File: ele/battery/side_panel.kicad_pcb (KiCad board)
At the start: 2 copper layers, 46.8 x 87.2 mm, 36 parts, among them J1 banana, J10 B1_trans, J11 B2_trans, J2 banana, J3 banana, J4 banana, J5 B1_sping, J6 B2_sping, J9 mech

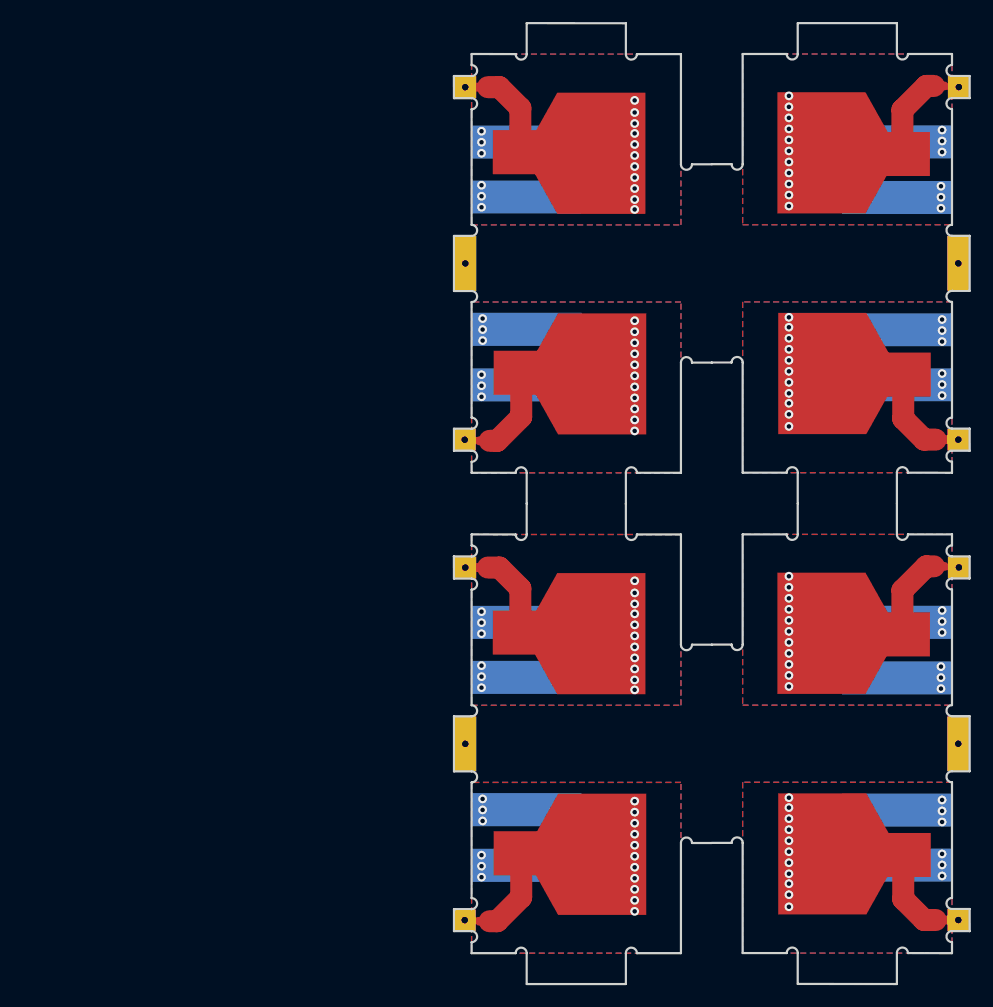
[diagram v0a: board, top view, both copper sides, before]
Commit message: ele: Update battery panels
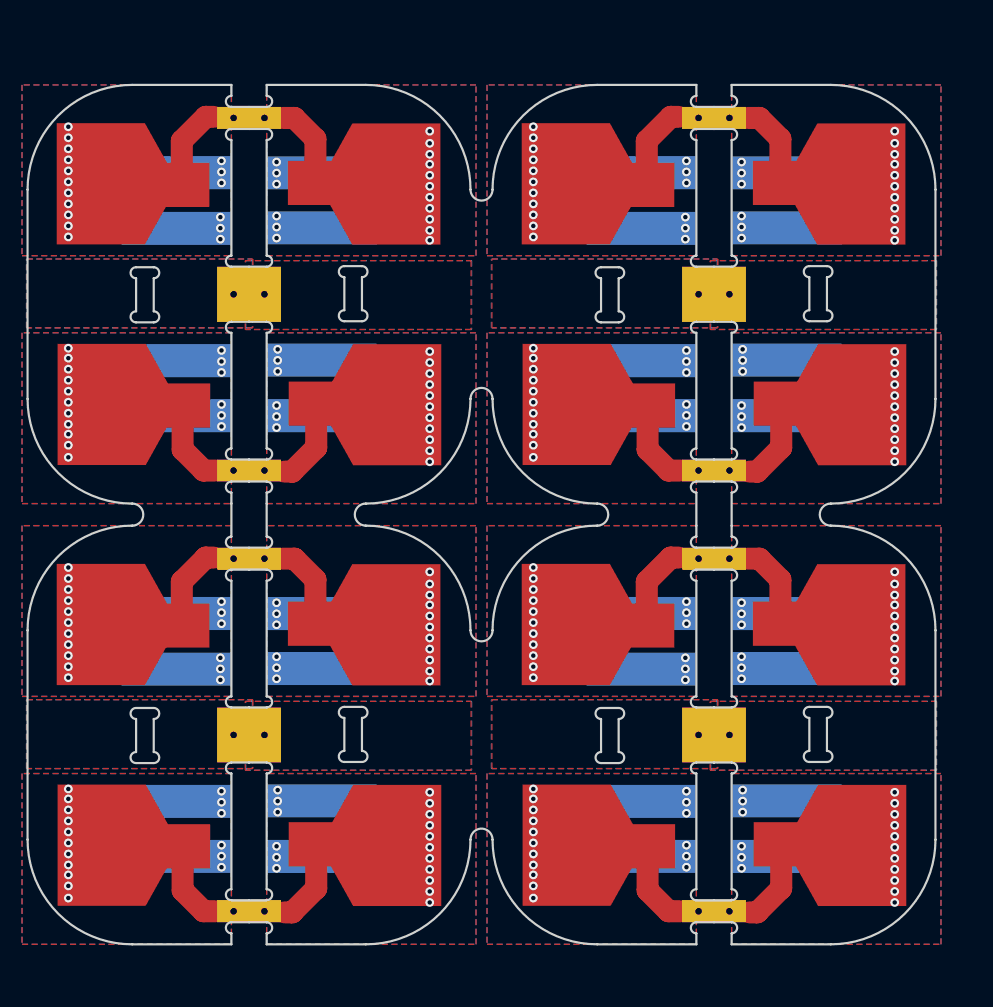
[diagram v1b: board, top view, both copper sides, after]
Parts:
- removed the J1 at (145.8, 141.2)
- removed the J1 at (112.2, 129.2)
- removed the J1 at (145.8, 97.6)
- removed the J1 at (112.2, 85.6)
- removed the J10 at (106.6, 119.2)
- removed the J10 at (151.4, 151.2)
- removed the J10 at (151.4, 107.6)
- removed the J10 at (106.6, 75.6)
- removed the J11 at (106.6, 151.2)
- removed the J11 at (151.4, 119.2)
- removed the J11 at (151.4, 75.6)
- removed the J11 at (106.6, 107.6)
- removed the J2 at (145.8, 146.2)
- removed the J2 at (112.2, 124.2)
- removed the J2 at (145.8, 102.6)
- removed the J2 at (112.2, 80.6)
- removed the J3 at (112.2, 146.2)
- removed the J3 at (145.8, 124.2)
- removed the J3 at (145.8, 80.6)
- removed the J3 at (112.2, 102.6)
- removed the J4 at (145.8, 129.2)
- removed the J4 at (112.2, 141.2)
- removed the J4 at (145.8, 85.6)
- removed the J4 at (112.2, 97.6)
- removed the J5 at (140.6, 145.3)
- removed the J5 at (117.4, 125.1)
- removed the J5 at (140.6, 101.7)
- removed the J5 at (117.4, 81.5)
- removed the J6 at (117.5, 145.1)
- removed the J6 at (140.5, 125.3)
- removed the J6 at (140.5, 81.7)
- removed the J6 at (117.5, 101.5)
- removed the J9 at (106.6, 135.2)
- removed the J9 at (151.4, 135.2)
- removed the J9 at (151.4, 91.6)
- removed the J9 at (106.6, 91.6)
- added J1: banana, yaqwsx:banana_2mm_side, B.Cu at (80.4, 100.4)
- added J1: banana, yaqwsx:banana_2mm_side, B.Cu at (93.6, 88.4)
- added J1: banana, yaqwsx:banana_2mm_side, B.Cu at (93.6, 128.4)
- added J1: banana, yaqwsx:banana_2mm_side, B.Cu at (80.4, 140.4)
- added J1: banana, yaqwsx:banana_2mm_side, B.Cu at (135.8, 128.4)
- added J1: banana, yaqwsx:banana_2mm_side, B.Cu at (122.6, 140.4)
- added J1: banana, yaqwsx:banana_2mm_side, B.Cu at (122.6, 100.4)
- added J1: banana, yaqwsx:banana_2mm_side, B.Cu at (135.8, 88.4)
- added J10: B1_trans, yaqwsx:pad_2x3, F.Cu at (85.6, 110.4)
- added J10: B1_trans, yaqwsx:pad_2x3, F.Cu at (88.4, 78.4)
- added J10: B1_trans, yaqwsx:pad_2x3, F.Cu at (88.4, 118.4)
- added J10: B1_trans, yaqwsx:pad_2x3, F.Cu at (85.6, 150.4)
- added J10: B1_trans, yaqwsx:pad_2x3, F.Cu at (130.6, 118.4)
- added J10: B1_trans, yaqwsx:pad_2x3, F.Cu at (127.8, 150.4)
- added J10: B1_trans, yaqwsx:pad_2x3, F.Cu at (127.8, 110.4)
- added J10: B1_trans, yaqwsx:pad_2x3, F.Cu at (130.6, 78.4)
- added J11: B2_trans, yaqwsx:pad_2x3, F.Cu at (85.6, 78.4)
- added J11: B2_trans, yaqwsx:pad_2x3, F.Cu at (88.4, 110.4)
- added J11: B2_trans, yaqwsx:pad_2x3, F.Cu at (88.4, 150.4)
- added J11: B2_trans, yaqwsx:pad_2x3, F.Cu at (85.6, 118.4)
- added J11: B2_trans, yaqwsx:pad_2x3, F.Cu at (130.6, 150.4)
- added J11: B2_trans, yaqwsx:pad_2x3, F.Cu at (127.8, 118.4)
- added J11: B2_trans, yaqwsx:pad_2x3, F.Cu at (127.8, 78.4)
- added J11: B2_trans, yaqwsx:pad_2x3, F.Cu at (130.6, 110.4)
- added J2: banana, yaqwsx:banana_2mm_side, B.Cu at (93.6, 83.4)
- added J2: banana, yaqwsx:banana_2mm_side, B.Cu at (80.4, 105.4)
- added J2: banana, yaqwsx:banana_2mm_side, B.Cu at (80.4, 145.4)
- added J2: banana, yaqwsx:banana_2mm_side, B.Cu at (93.6, 123.4)
- added J2: banana, yaqwsx:banana_2mm_side, B.Cu at (122.6, 145.4)
- added J2: banana, yaqwsx:banana_2mm_side, B.Cu at (135.8, 123.4)
- added J2: banana, yaqwsx:banana_2mm_side, B.Cu at (122.6, 105.4)
- added J2: banana, yaqwsx:banana_2mm_side, B.Cu at (135.8, 83.4)
- added J3: banana, yaqwsx:banana_2mm_side, B.Cu at (80.4, 83.4)
- added J3: banana, yaqwsx:banana_2mm_side, B.Cu at (93.6, 145.4)
- added J3: banana, yaqwsx:banana_2mm_side, B.Cu at (93.6, 105.4)
- added J3: banana, yaqwsx:banana_2mm_side, B.Cu at (80.4, 123.4)
- added J3: banana, yaqwsx:banana_2mm_side, B.Cu at (135.8, 145.4)
- added J3: banana, yaqwsx:banana_2mm_side, B.Cu at (122.6, 123.4)
- added J3: banana, yaqwsx:banana_2mm_side, B.Cu at (122.6, 83.4)
- added J3: banana, yaqwsx:banana_2mm_side, B.Cu at (135.8, 105.4)
- added J4: banana, yaqwsx:banana_2mm_side, B.Cu at (80.4, 88.4)
- added J4: banana, yaqwsx:banana_2mm_side, B.Cu at (93.6, 100.4)
- added J4: banana, yaqwsx:banana_2mm_side, B.Cu at (93.6, 140.4)
- added J4: banana, yaqwsx:banana_2mm_side, B.Cu at (80.4, 128.4)
- added J4: banana, yaqwsx:banana_2mm_side, B.Cu at (135.8, 140.4)
- added J4: banana, yaqwsx:banana_2mm_side, B.Cu at (122.6, 128.4)
- added J4: banana, yaqwsx:banana_2mm_side, B.Cu at (122.6, 88.4)
- added J4: banana, yaqwsx:banana_2mm_side, B.Cu at (135.8, 100.4)
- added J5: B1_sping, yaqwsx:battery_spring_contact, F.Cu at (98.8, 84.3)
- added J5: B1_sping, yaqwsx:battery_spring_contact, F.Cu at (75.2, 104.5)
- added J5: B1_sping, yaqwsx:battery_spring_contact, F.Cu at (98.8, 124.3)
- added J5: B1_sping, yaqwsx:battery_spring_contact, F.Cu at (75.2, 144.5)
- added J5: B1_sping, yaqwsx:battery_spring_contact, F.Cu at (141.0, 124.3)
- added J5: B1_sping, yaqwsx:battery_spring_contact, F.Cu at (117.4, 144.5)
- added J5: B1_sping, yaqwsx:battery_spring_contact, F.Cu at (117.4, 104.5)
- added J5: B1_sping, yaqwsx:battery_spring_contact, F.Cu at (141.0, 84.3)
- added J6: B2_sping, yaqwsx:battery_spring_contact, F.Cu at (75.1, 84.5)
- added J6: B2_sping, yaqwsx:battery_spring_contact, F.Cu at (98.9, 104.3)
- added J6: B2_sping, yaqwsx:battery_spring_contact, F.Cu at (98.9, 144.3)
- added J6: B2_sping, yaqwsx:battery_spring_contact, F.Cu at (75.1, 124.5)
- added J6: B2_sping, yaqwsx:battery_spring_contact, F.Cu at (141.1, 144.3)
- added J6: B2_sping, yaqwsx:battery_spring_contact, F.Cu at (117.3, 124.5)
- added J6: B2_sping, yaqwsx:battery_spring_contact, F.Cu at (117.3, 84.5)
- added J6: B2_sping, yaqwsx:battery_spring_contact, F.Cu at (141.1, 104.3)
- added J9: mech, BATTERY:pad_3x5, F.Cu at (88.4, 94.4)
- added J9: mech, BATTERY:pad_3x5, F.Cu at (85.6, 94.4)
- added J9: mech, BATTERY:pad_3x5, F.Cu at (85.6, 134.4)
- added J9: mech, BATTERY:pad_3x5, F.Cu at (88.4, 134.4)
- added J9: mech, BATTERY:pad_3x5, F.Cu at (127.8, 134.4)
- added J9: mech, BATTERY:pad_3x5, F.Cu at (130.6, 134.4)
- added J9: mech, BATTERY:pad_3x5, F.Cu at (127.8, 94.4)
- added J9: mech, BATTERY:pad_3x5, F.Cu at (130.6, 94.4)
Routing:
- net /B1_trans: track 76.7 -> 153.4 mm, vias 44 -> 88
- net /B2_trans: track 49.5 -> 99.0 mm, vias 44 -> 88
- net Net-(J4-Pad1): vias 12 -> 24
- net Net-(J3-Pad1): vias 12 -> 24
- net Net-(J2-Pad1): vias 12 -> 24
- net Net-(J1-Pad1): vias 12 -> 24
- added copper zone on B.Cu, net Net-(J9-Pad1)
- added copper zone on F.Cu, net Net-(J9-Pad1)
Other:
- board size 46.8 x 87.2 mm -> 82.4 x 78 mm

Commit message: ele: Update battery panels
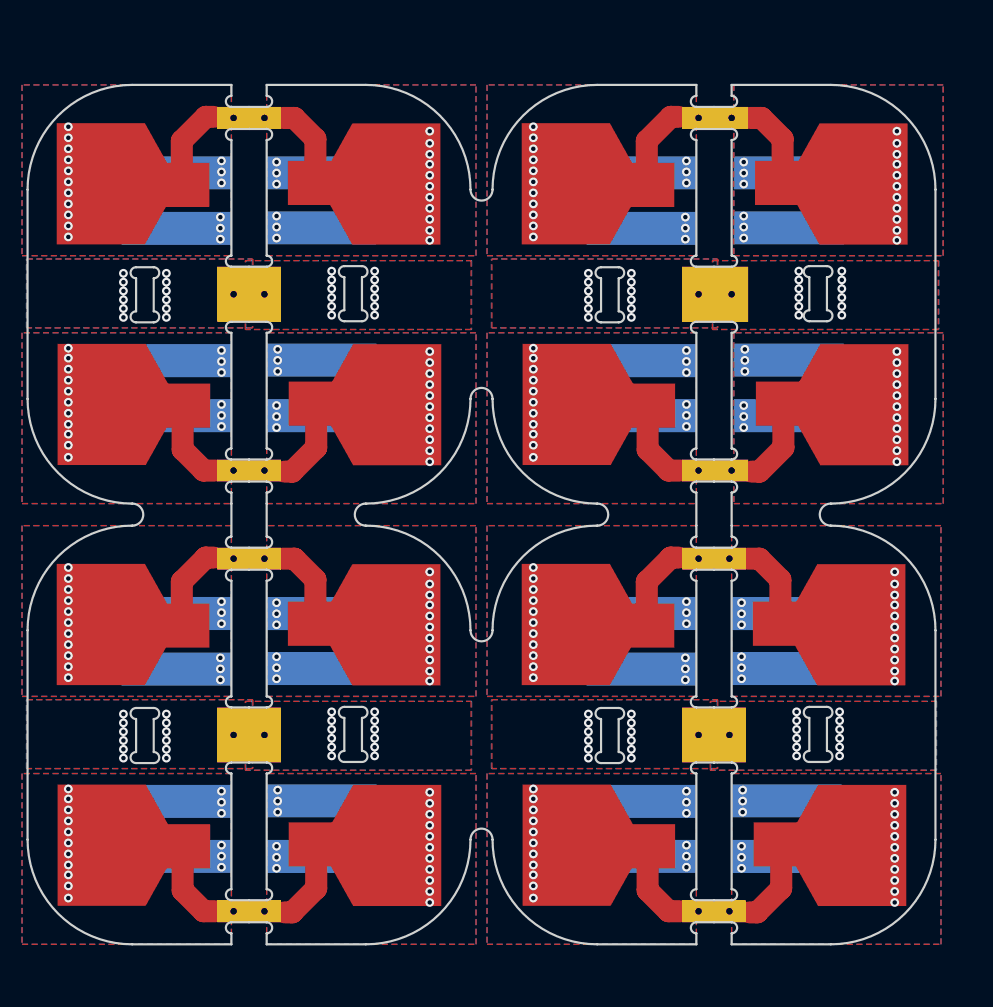
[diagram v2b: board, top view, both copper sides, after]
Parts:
- moved J10 0.20 mm to (130.8, 78.4)
- moved J11 0.20 mm to (130.8, 110.4)
- moved J6 0.20 mm to (141.3, 104.3)
- moved J9 0.20 mm to (130.8, 94.4)
- moved J1 0.20 mm to (136.0, 88.4)
- moved J2 0.20 mm to (136.0, 83.4)
- moved J3 0.20 mm to (136.0, 105.4)
- moved J4 0.20 mm to (136.0, 100.4)
- moved J5 0.20 mm to (141.2, 84.3)
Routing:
- net Net-(J9-Pad1): vias 0 -> 96

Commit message: ele: Remove potential short-circuit in a battery
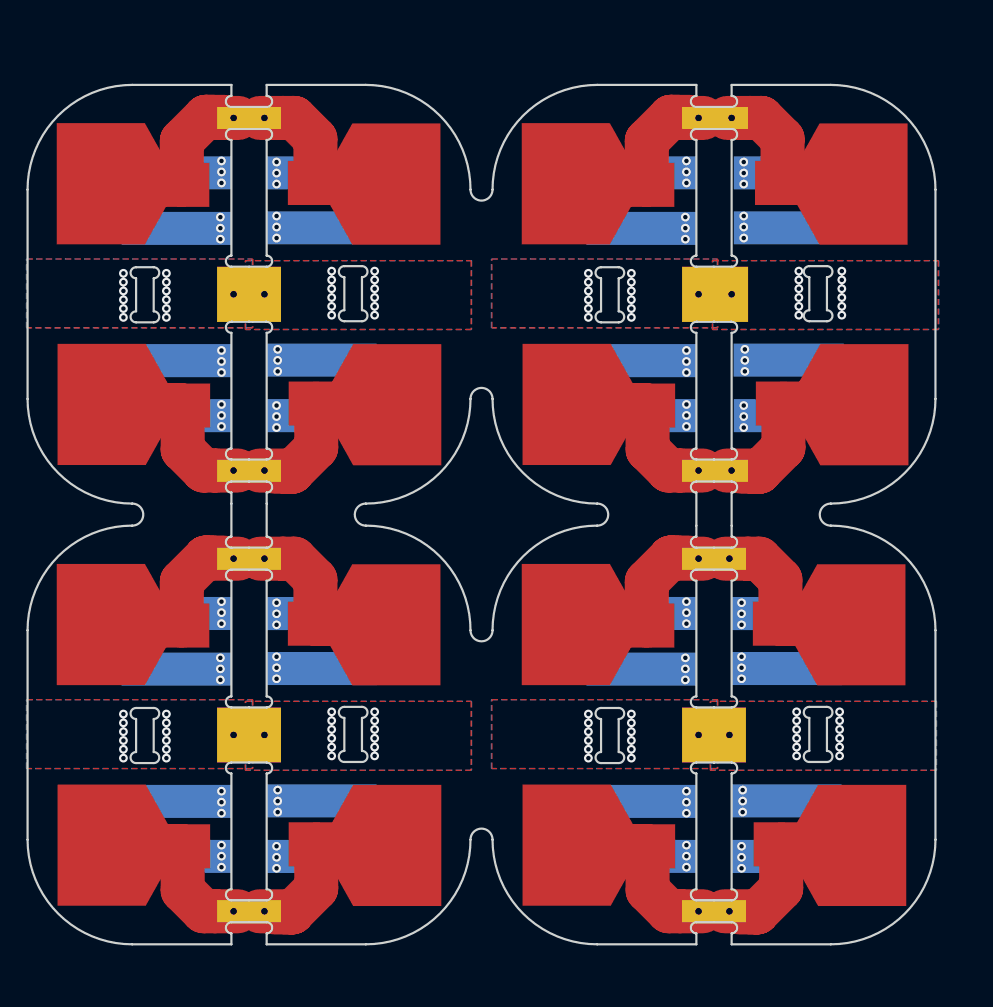
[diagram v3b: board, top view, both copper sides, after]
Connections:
- J10 pad 1: /B1_trans -> /B2_trans
- J11 pad 1: /B2_trans -> /B1_trans
- J5 pad 1: /B1_trans -> /B2_trans
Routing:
- net /B1_trans: track 153.4 -> 146.6 mm, vias 88 -> 0
- net /B2_trans: track 99.0 -> 105.8 mm, vias 88 -> 0
- removed copper zone on B.Cu, net /B1_trans
- removed copper zone on F.Cu, net /B1_trans
- removed copper zone on B.Cu, net /B2_trans
- removed copper zone on F.Cu, net /B2_trans
